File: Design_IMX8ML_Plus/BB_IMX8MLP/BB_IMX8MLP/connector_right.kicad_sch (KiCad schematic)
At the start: 4 parts, among them J3 Front_Left, J4 Back_Left

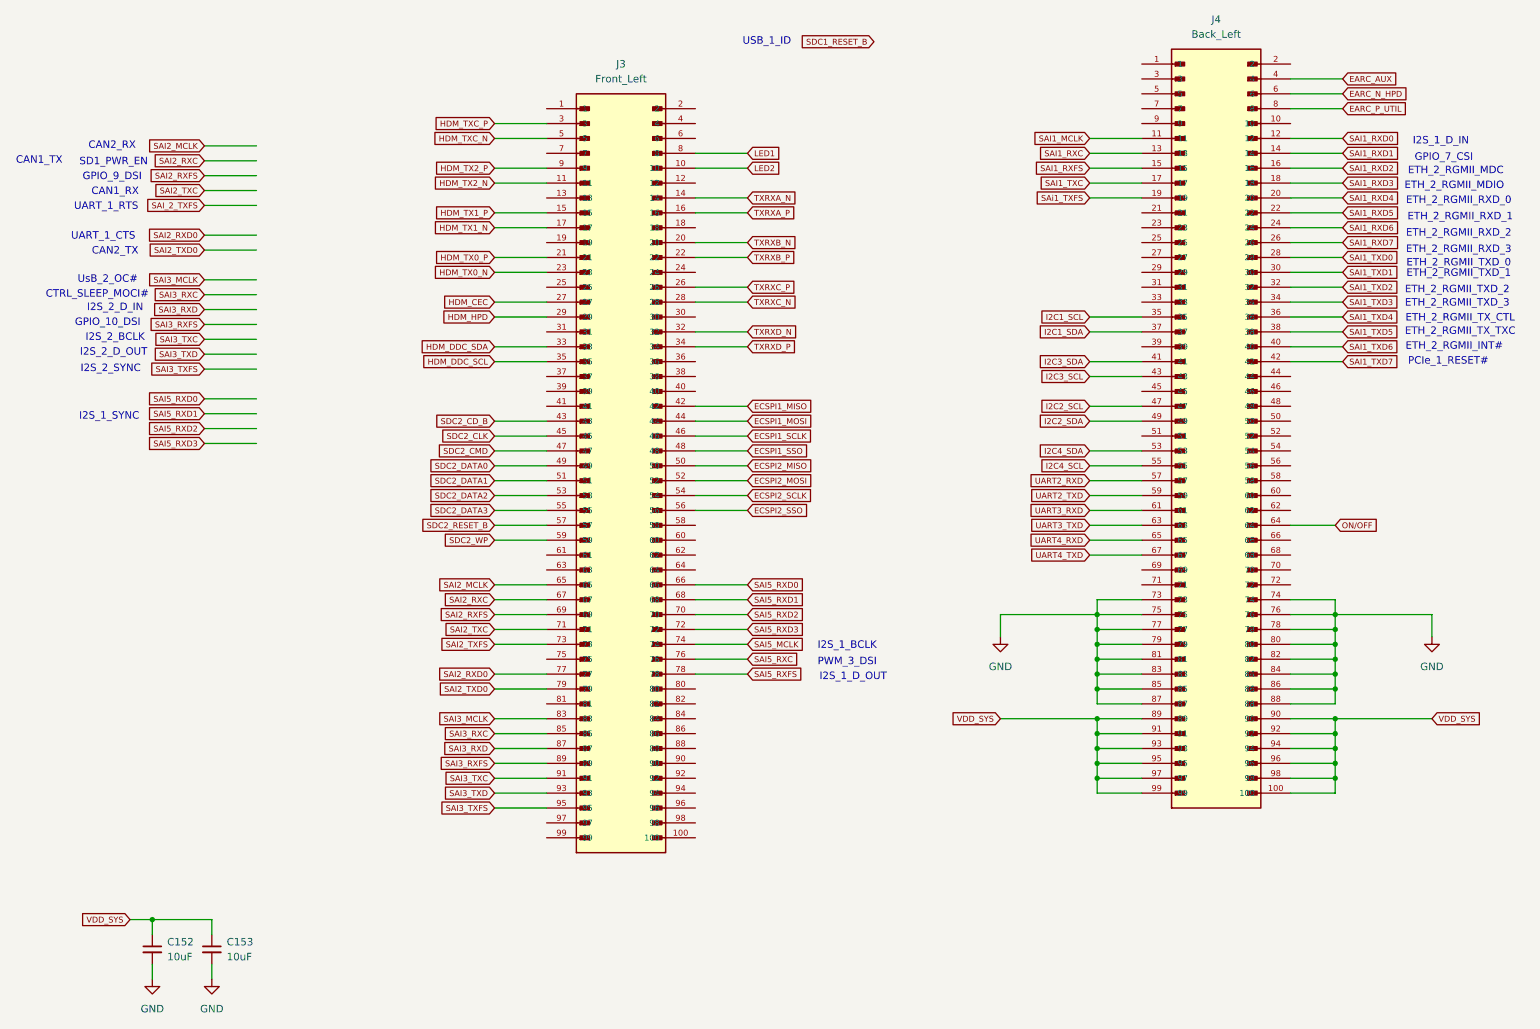
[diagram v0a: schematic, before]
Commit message: [PROCESSOR] Create zones It added power zones in the four layer
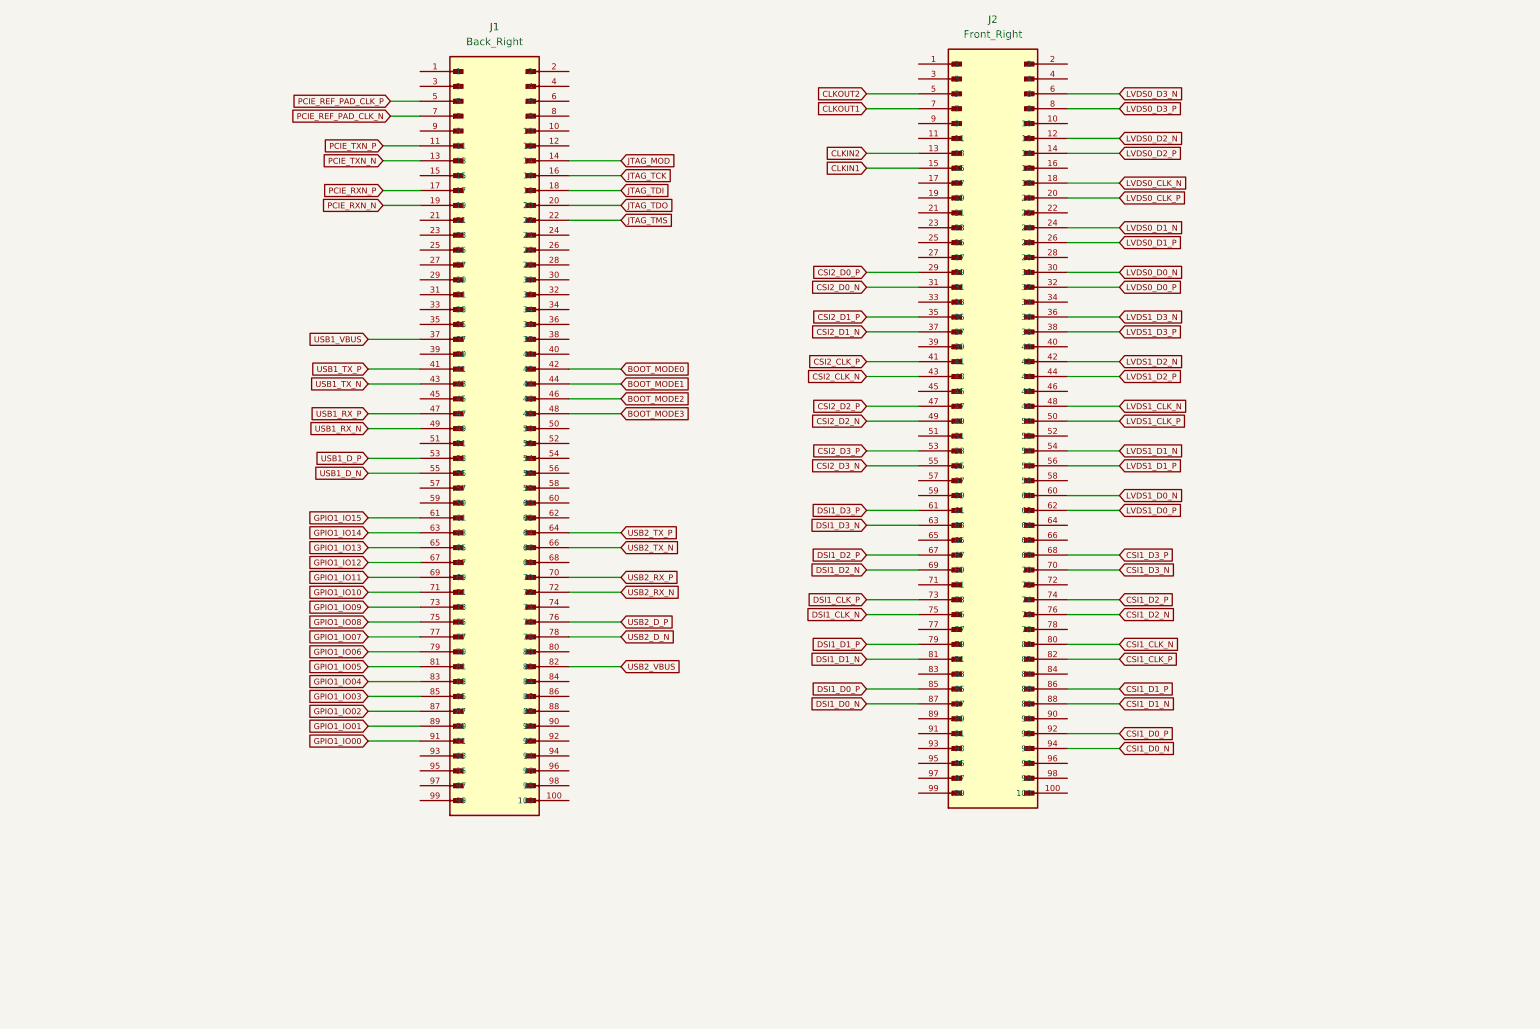
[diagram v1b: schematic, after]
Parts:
- removed C152, C153: 10uF, Capacitor_SMD:C_0603_1608Metric, symbol Device:C_Small
- removed J3: Front_Left, _W_SBC:HIROSE_DF40C-100DS-0.4V_51_, symbol CONN_DF40C-100DS-0_4V51_HIR:DF40C-100DP-0.4V_51_
- removed J4: Back_Left, _W_SBC:HIROSE_DF40C-100DS-0.4V_51_, symbol CONN_DF40C-100DS-0_4V51_HIR:DF40C-100DP-0.4V_51_
- added J1: Back_Right, _W_SBC:HIROSE_DF40C-100DS-0.4V_51_, symbol CONN_DF40C-100DS-0_4V51_HIR:DF40C-100DP-0.4V_51_
- added J2: Front_Right, _W_SBC:HIROSE_DF40C-100DS-0.4V_51_, symbol CONN_DF40C-100DS-0_4V51_HIR:DF40C-100DP-0.4V_51_
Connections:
- new net BOOT_MODE0: J1.42
- new net BOOT_MODE1: J1.44
- new net BOOT_MODE2: J1.46
- new net BOOT_MODE3: J1.48
- new net CLKIN1: J2.15
- new net CLKIN2: J2.13
- new net CLKOUT1: J2.7
- new net CLKOUT2: J2.5
- new net CSI1_CLK_N: J2.80
- new net CSI1_CLK_P: J2.82
- new net CSI1_D0_N: J2.94
- new net CSI1_D0_P: J2.92
- new net CSI1_D1_N: J2.88
- new net CSI1_D1_P: J2.86
- new net CSI1_D2_N: J2.76
- new net CSI1_D2_P: J2.74
- new net CSI1_D3_N: J2.70
- new net CSI1_D3_P: J2.68
- new net CSI2_CLK_N: J2.43
- new net CSI2_CLK_P: J2.41
- new net CSI2_D0_N: J2.31
- new net CSI2_D0_P: J2.29
- new net CSI2_D1_N: J2.37
- new net CSI2_D1_P: J2.35
- new net CSI2_D2_N: J2.49
- new net CSI2_D2_P: J2.47
- new net CSI2_D3_N: J2.55
- new net CSI2_D3_P: J2.53
- new net DSI1_CLK_N: J2.75
- new net DSI1_CLK_P: J2.73
- new net DSI1_D0_N: J2.87
- new net DSI1_D0_P: J2.85
- new net DSI1_D1_N: J2.81
- new net DSI1_D1_P: J2.79
- new net DSI1_D2_N: J2.69
- new net DSI1_D2_P: J2.67
- new net DSI1_D3_N: J2.63
- new net DSI1_D3_P: J2.61
- new net GPIO1_IO00: J1.91
- new net GPIO1_IO01: J1.89
- new net GPIO1_IO02: J1.87
- new net GPIO1_IO03: J1.85
- new net GPIO1_IO04: J1.83
- new net GPIO1_IO05: J1.81
- new net GPIO1_IO06: J1.79
- new net GPIO1_IO07: J1.77
- new net GPIO1_IO08: J1.75
- new net GPIO1_IO09: J1.73
- new net GPIO1_IO10: J1.71
- new net GPIO1_IO11: J1.69
- new net GPIO1_IO12: J1.67
- new net GPIO1_IO13: J1.65
- new net GPIO1_IO14: J1.63
- new net GPIO1_IO15: J1.61
- new net JTAG_MOD: J1.14
- new net JTAG_TCK: J1.16
- new net JTAG_TDI: J1.18
- new net JTAG_TDO: J1.20
- new net JTAG_TMS: J1.22
- new net LVDS0_CLK_N: J2.18
- new net LVDS0_CLK_P: J2.20
- new net LVDS0_D0_N: J2.30
- new net LVDS0_D0_P: J2.32
- new net LVDS0_D1_N: J2.24
- new net LVDS0_D1_P: J2.26
- new net LVDS0_D2_N: J2.12
- new net LVDS0_D2_P: J2.14
- new net LVDS0_D3_N: J2.6
- new net LVDS0_D3_P: J2.8
- new net LVDS1_CLK_N: J2.48
- new net LVDS1_CLK_P: J2.50
- new net LVDS1_D0_N: J2.60
- new net LVDS1_D0_P: J2.62
- new net LVDS1_D1_N: J2.54
- new net LVDS1_D1_P: J2.56
- new net LVDS1_D2_N: J2.42
- new net LVDS1_D2_P: J2.44
- new net LVDS1_D3_N: J2.36
- new net LVDS1_D3_P: J2.38
- new net PCIE_REF_PAD_CLK_N: J1.7
- new net PCIE_REF_PAD_CLK_P: J1.5
- new net PCIE_RXN_N: J1.19
- new net PCIE_RXN_P: J1.17
- new net PCIE_TXN_N: J1.13
- new net PCIE_TXN_P: J1.11
- new net USB1_D_N: J1.55
- new net USB1_D_P: J1.53
- new net USB1_RX_N: J1.49
- new net USB1_RX_P: J1.47
- new net USB1_TX_N: J1.43
- new net USB1_TX_P: J1.41
- new net USB1_VBUS: J1.37
- new net USB2_D_N: J1.78
- new net USB2_D_P: J1.76
- new net USB2_RX_N: J1.72
- new net USB2_RX_P: J1.70
- new net USB2_TX_N: J1.66
- new net USB2_TX_P: J1.64
- new net USB2_VBUS: J1.82
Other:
- note removed: "CAN1_RX"
- note removed: "CAN1_TX"
- note removed: "CAN2_RX"
- note removed: "CAN2_TX"
- note removed: "CTRL_SLEEP_MOCI#"
- note removed: "ETH_2_RGMII_INT#"
- note removed: "ETH_2_RGMII_MDC"
- note removed: "ETH_2_RGMII_MDIO"
- note removed: "ETH_2_RGMII_RXD_0"
- note removed: "ETH_2_RGMII_RXD_1"
- note removed: "ETH_2_RGMII_RXD_2"
- note removed: "ETH_2_RGMII_RXD_3"
- note removed: "ETH_2_RGMII_TXD_0"
- note removed: "ETH_2_RGMII_TXD_1"
- note removed: "ETH_2_RGMII_TXD_2"
- note removed: "ETH_2_RGMII_TXD_3"
- note removed: "ETH_2_RGMII_TX_CTL"
- note removed: "ETH_2_RGMII_TX_TXC"
- note removed: "GPIO_10_DSI"
- note removed: "GPIO_7_CSI"
- note removed: "GPIO_9_DSI"
- note removed: "I2S_1_BCLK"
- note removed: "I2S_1_D_IN"
- note removed: "I2S_1_D_OUT"
- note removed: "I2S_1_SYNC"
- note removed: "I2S_2_BCLK"
- note removed: "I2S_2_D_IN"
- note removed: "I2S_2_D_OUT"
- note removed: "I2S_2_SYNC"
- note removed: "PCIe_1_RESET#"
- note removed: "PWM_3_DSI"
- note removed: "SD1_PWR_EN"
- note removed: "UART_1_CTS"
- note removed: "UART_1_RTS"
- note removed: "USB_1_ID"
- note removed: "UsB_2_OC#"

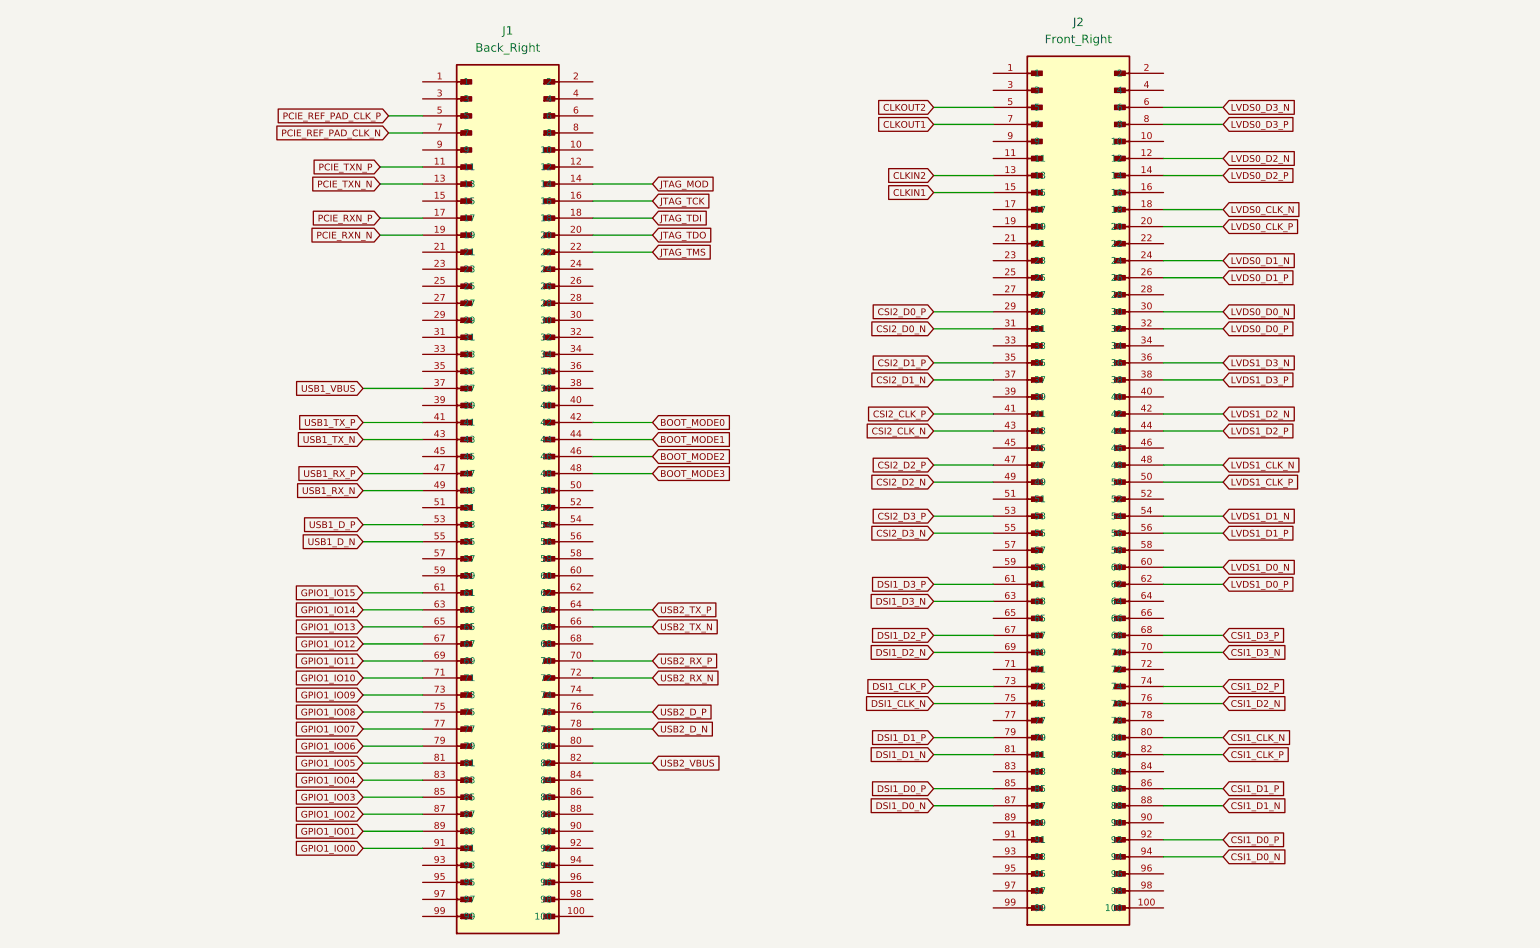
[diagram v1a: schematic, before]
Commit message: [CPU/BB] Improving the conection between the cpu and BB
* Reorganization of the components in the Base board.
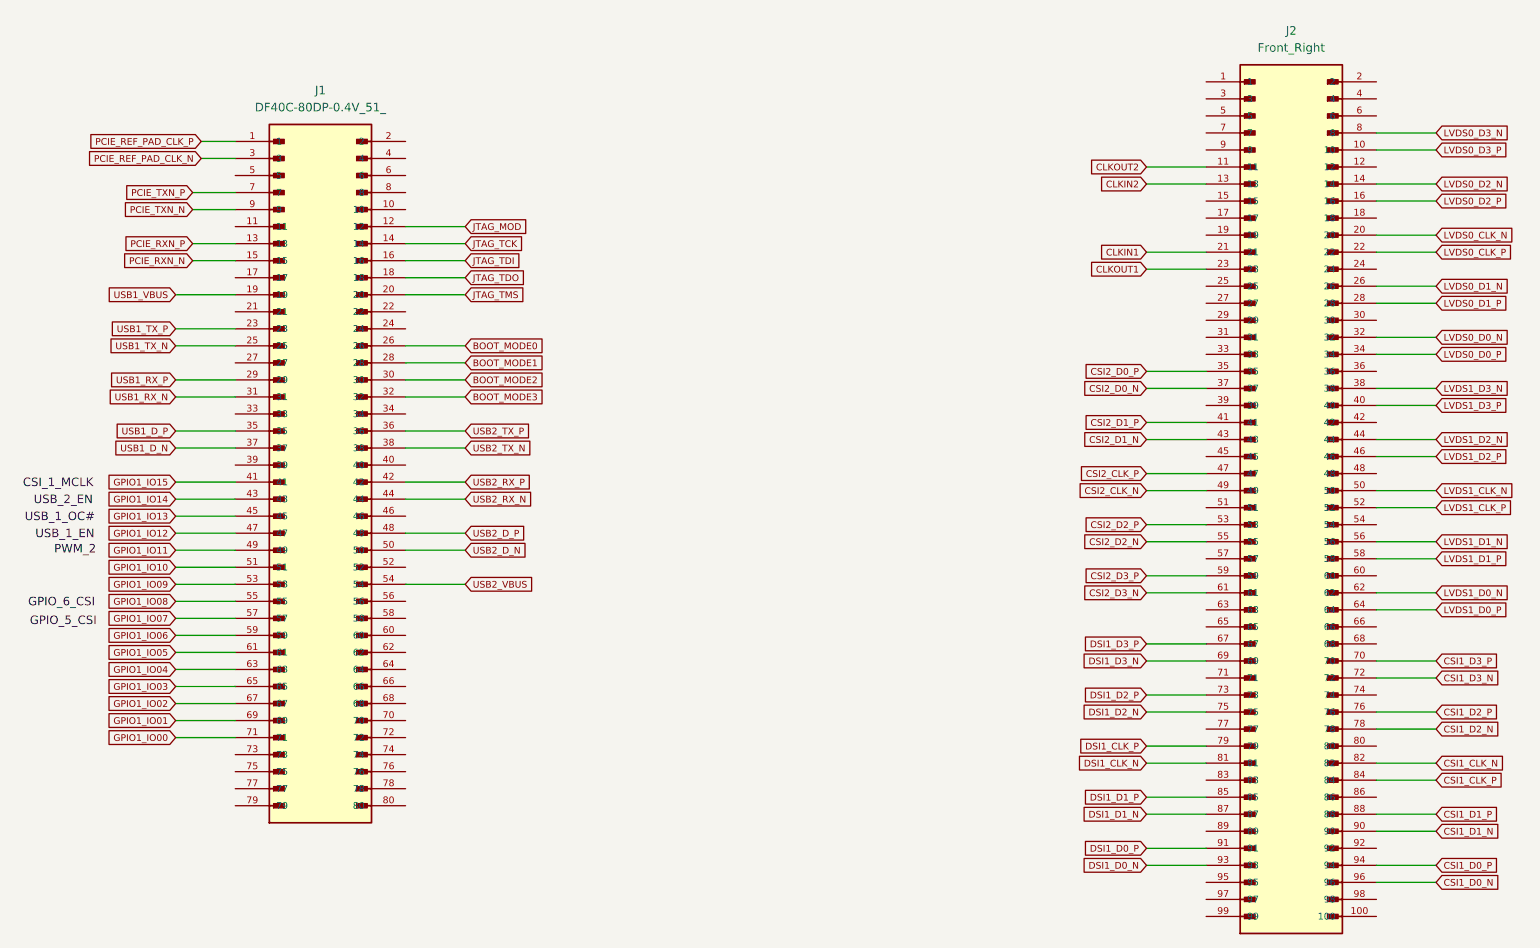
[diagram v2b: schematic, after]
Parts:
- removed J1: Back_Right, _W_SBC:HIROSE_DF40C-100DS-0.4V_51_, symbol CONN_DF40C-100DS-0_4V51_HIR:DF40C-100DP-0.4V_51_
- added J1: DF40C-80DP-0.4V_51_, _W_SBC:HRS_DF40C-80DS-0.4V_51_, symbol DF40C-80DP-0.4V_51_:DF40C-80DP-0.4V_51_
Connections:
- net BOOT_MODE0: now also J1.26
- net BOOT_MODE1: now also J1.28
- net BOOT_MODE2: now also J1.30
- net BOOT_MODE3: now also J1.32
- net CLKIN1: now also J2.21; no longer J2.15
- net CLKOUT1: now also J2.23; no longer J2.7
- net CLKOUT2: now also J2.11; no longer J2.5
- net CSI1_CLK_N: now also J2.82; no longer J2.80
- net CSI1_CLK_P: now also J2.84; no longer J2.82
- net CSI1_D0_N: now also J2.96; no longer J2.94
- net CSI1_D0_P: now also J2.94; no longer J2.92
- net CSI1_D1_N: now also J2.90; no longer J2.88
- net CSI1_D1_P: now also J2.88; no longer J2.86
- net CSI1_D2_N: now also J2.78; no longer J2.76
- net CSI1_D2_P: now also J2.76; no longer J2.74
- net CSI1_D3_N: now also J2.72; no longer J2.70
- net CSI1_D3_P: now also J2.70; no longer J2.68
- net CSI2_CLK_N: now also J2.49; no longer J2.43
- net CSI2_CLK_P: now also J2.47; no longer J2.41
- net CSI2_D0_N: now also J2.37; no longer J2.31
- net CSI2_D0_P: now also J2.35; no longer J2.29
- net CSI2_D1_N: now also J2.43; no longer J2.37
- net CSI2_D1_P: now also J2.41; no longer J2.35
- net CSI2_D2_N: now also J2.55; no longer J2.49
- net CSI2_D2_P: now also J2.53; no longer J2.47
- net CSI2_D3_N: now also J2.61; no longer J2.55
- net CSI2_D3_P: now also J2.59; no longer J2.53
- net DSI1_CLK_N: now also J2.81; no longer J2.75
- net DSI1_CLK_P: now also J2.79; no longer J2.73
- net DSI1_D0_N: now also J2.93; no longer J2.87
- net DSI1_D0_P: now also J2.91; no longer J2.85
- net DSI1_D1_N: now also J2.87; no longer J2.81
- net DSI1_D1_P: now also J2.85; no longer J2.79
- net DSI1_D2_N: now also J2.75; no longer J2.69
- net DSI1_D2_P: now also J2.73; no longer J2.67
- net DSI1_D3_N: now also J2.69; no longer J2.63
- net DSI1_D3_P: now also J2.67; no longer J2.61
- net GPIO1_IO00: now also J1.71
- net GPIO1_IO01: now also J1.69
- net GPIO1_IO02: now also J1.67
- net GPIO1_IO03: now also J1.65
- net GPIO1_IO04: now also J1.63
- net GPIO1_IO05: now also J1.61
- net GPIO1_IO06: now also J1.59
- net GPIO1_IO07: now also J1.57
- net GPIO1_IO08: now also J1.55
- net GPIO1_IO09: now also J1.53
- net GPIO1_IO10: now also J1.51
- net GPIO1_IO11: now also J1.49
- net GPIO1_IO12: now also J1.47
- net GPIO1_IO13: now also J1.45
- net GPIO1_IO14: now also J1.43
- net GPIO1_IO15: now also J1.41
- net JTAG_MOD: now also J1.12
- net JTAG_TCK: now also J1.14
- net JTAG_TDI: now also J1.16
- net JTAG_TDO: now also J1.18
- net JTAG_TMS: now also J1.20
- net LVDS0_CLK_N: now also J2.20; no longer J2.18
- net LVDS0_CLK_P: now also J2.22; no longer J2.20
- net LVDS0_D0_N: now also J2.32; no longer J2.30
- net LVDS0_D0_P: now also J2.34; no longer J2.32
- net LVDS0_D1_N: now also J2.26; no longer J2.24
- net LVDS0_D1_P: now also J2.28; no longer J2.26
- net LVDS0_D2_N: now also J2.14; no longer J2.12
- net LVDS0_D2_P: now also J2.16; no longer J2.14
- net LVDS0_D3_N: now also J2.8; no longer J2.6
- net LVDS0_D3_P: now also J2.10; no longer J2.8
- net LVDS1_CLK_N: now also J2.50; no longer J2.48
- net LVDS1_CLK_P: now also J2.52; no longer J2.50
- net LVDS1_D0_N: now also J2.62; no longer J2.60
- net LVDS1_D0_P: now also J2.64; no longer J2.62
- net LVDS1_D1_N: now also J2.56; no longer J2.54
- net LVDS1_D1_P: now also J2.58; no longer J2.56
- net LVDS1_D2_N: now also J2.44; no longer J2.42
- net LVDS1_D2_P: now also J2.46; no longer J2.44
- net LVDS1_D3_N: now also J2.38; no longer J2.36
- net LVDS1_D3_P: now also J2.40; no longer J2.38
- net PCIE_REF_PAD_CLK_N: now also J1.3
- net PCIE_REF_PAD_CLK_P: now also J1.1
- net PCIE_RXN_N: now also J1.15
- net PCIE_RXN_P: now also J1.13
- net PCIE_TXN_N: now also J1.9
- net PCIE_TXN_P: now also J1.7
- net USB1_D_N: now also J1.37
- net USB1_D_P: now also J1.35
- net USB1_RX_N: now also J1.31
- net USB1_RX_P: now also J1.29
- net USB1_TX_N: now also J1.25
- net USB1_TX_P: now also J1.23
- net USB1_VBUS: now also J1.19
- net USB2_D_N: now also J1.50
- net USB2_D_P: now also J1.48
- net USB2_RX_N: now also J1.44
- net USB2_RX_P: now also J1.42
- net USB2_TX_N: now also J1.38
- net USB2_TX_P: now also J1.36
- net USB2_VBUS: now also J1.54
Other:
- note added: "CSI_1_MCLK"
- note added: "GPIO_5_CSI"
- note added: "GPIO_6_CSI"
- note added: "PWM_2"
- note added: "USB_1_EN"
- note added: "USB_1_OC#"
- note added: "USB_2_EN"
- moved on the sheet: J2
